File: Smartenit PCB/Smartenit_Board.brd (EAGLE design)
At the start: 55.3 x 72.5 mm, 85 parts, among them J3 2X5CONNECTOR1.27MM, Q1 QUARTZ_3.58M_2PIN, U1 ADE7953, U2 ESP-WROOM-32, U3 SN74LVC1G3157

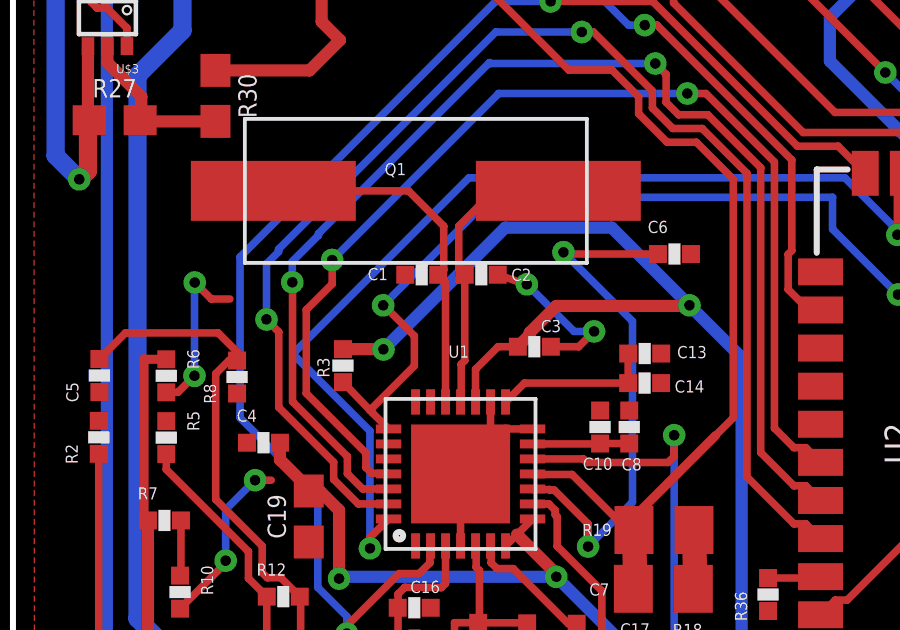
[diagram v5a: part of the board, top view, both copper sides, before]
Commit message: moved two caps
proximity issue reslved with caps by crystal.
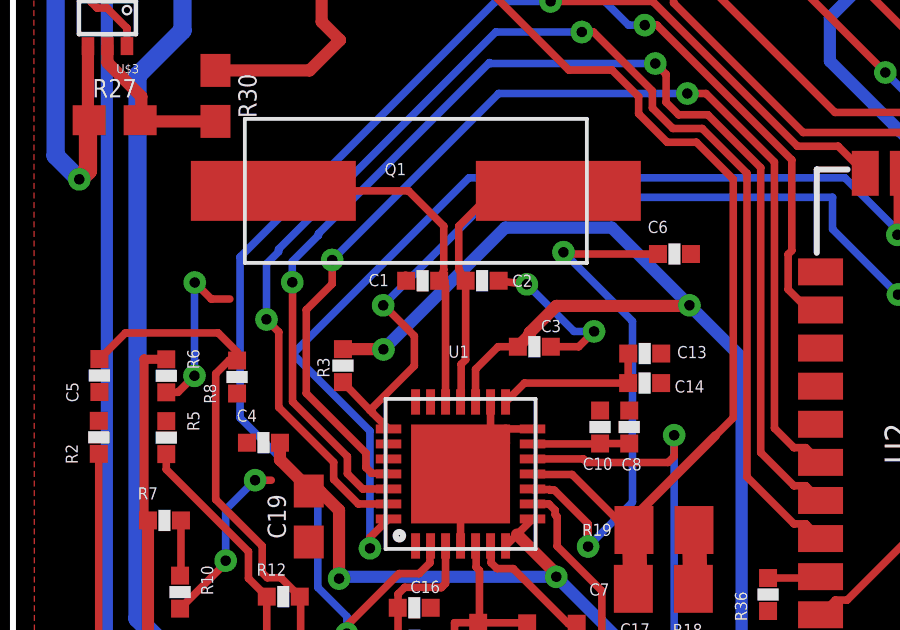
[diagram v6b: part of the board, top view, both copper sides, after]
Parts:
- moved C1 0.20 mm to (13.7, -29.2)
- moved C2 0.20 mm to (15.6, -29.2)
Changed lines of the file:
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@@
 <attribute name="NAME" x="12.39" y="-25.695" size="0.4064" layer="21"/>
 </element>
-<element name="C1" library="Nizanlib" package="0402-CAP" value="20p" x="13.626" y="-29.012" smashed="yes">
-<attribute name="NAME" x="11.827" y="-29.1935" size="0.4064" layer="25"/>
-</element>
-<element name="C2" library="Nizanlib" package="0402-CAP" value="20p" x="15.61" y="-29.01" smashed="yes" rot="R180">
-<attribute name="NAME" x="17.279" y="-28.8085" size="0.4064" layer="25" rot="R180"/>
+<element name="C1" library="Nizanlib" package="0402-CAP" value="20p" x="13.656" y="-29.212" smashed="yes">
+<attribute name="NAME" x="11.857" y="-29.3935" size="0.4064" layer="25"/>
+</element>
+<element name="C2" library="Nizanlib" package="0402-CAP" value="20p" x="15.64" y="-29.21" smashed="yes" rot="R180">
+<attribute name="NAME" x="17.309" y="-29.0085" size="0.4064" layer="25" rot="R180"/>
 </element>
 <element name="C8" library="Nizanlib" package="0402-CAP" value="475n" x="20.542" y="-34.087" smashed="yes" rot="R90">
@@
 <contactref element="Q1" pad="1"/>
 <wire x1="14.36" y1="-29.266" x2="14.196" y2="-29.102" width="0.254" layer="1"/>
-<wire x1="14.196" y1="-29.102" x2="14.176" y2="-29.012" width="0.254" layer="1"/>
+<wire x1="14.196" y1="-29.102" x2="14.206" y2="-29.212" width="0.254" layer="1"/>
 <wire x1="14.36" y1="-28.848" x2="14.36" y2="-27.39" width="0.254" layer="1"/>
-<wire x1="14.36" y1="-28.848" x2="14.176" y2="-29.012" width="0.254" layer="1"/>
+<wire x1="14.36" y1="-28.848" x2="14.206" y2="-29.212" width="0.254" layer="1"/>
 <wire x1="14.42" y1="-29.38455625" x2="14.42" y2="-33.251" width="0.254" layer="1"/>
-<wire x1="14.176" y1="-29.012" x2="14.393475" y2="-29.229475" width="0.254" layer="1"/>
+<wire x1="14.206" y1="-29.212" x2="14.393475" y2="-29.229475" width="0.254" layer="1"/>
 <wire x1="14.393475" y1="-29.229475" x2="14.393475" y2="-29.35803125" width="0.254" layer="1"/>
 <wire x1="14.393475" y1="-29.35803125" x2="14.42" y2="-29.38455625" width="0.254" layer="1"/>
@@
 <contactref element="C2" pad="2"/>
 <wire x1="14.86" y1="-28.83" x2="14.86" y2="-27.39" width="0.254" layer="1"/>
-<wire x1="14.86" y1="-28.83" x2="15.06" y2="-29.01" width="0.254" layer="1"/>
-<wire x1="14.86" y1="-29.19" x2="15.06" y2="-29.01" width="0.254" layer="1"/>
-<wire x1="15.06" y1="-29.01" x2="15.06" y2="-31.87341875" width="0.254" layer="1"/>
+<wire x1="14.86" y1="-28.83" x2="15.09" y2="-29.21" width="0.254" layer="1"/>
 <wire x1="14.9398" y1="-33.2312" x2="14.92" y2="-33.251" width="0.254" layer="1"/>
-<wire x1="15.06" y1="-31.87341875" x2="14.9398" y2="-31.99361875" width="0.254" layer="1"/>
 <wire x1="14.9398" y1="-31.99361875" x2="14.9398" y2="-33.2312" width="0.254" layer="1"/>
 <wire x1="14.86" y1="-27.39" x2="16.035" y2="-26.215" width="0.254" layer="1"/>
 <wire x1="16.035" y1="-26.215" x2="18.18" y2="-26.215" width="0.254" layer="1"/>
+<wire x1="15.09" y1="-29.21" x2="15.09" y2="-31.84341875" width="0.254" layer="1"/>
+<wire x1="15.09" y1="-31.84341875" x2="14.9398" y2="-31.99361875" width="0.254" layer="1"/>
 </signal>
 <signal name="N$7">
@@
 <contactref element="R11" pad="2"/>
 <wire x1="22.74" y1="-42.05" x2="22.62" y2="-41.93" width="0.254" layer="1"/>
-<wire x1="13.088" y1="-29.02" x2="13.076" y2="-29.012" width="0.254" layer="1"/>
+<wire x1="13.088" y1="-29.02" x2="13.106" y2="-29.212" width="0.254" layer="1"/>
 <contactref element="R1" pad="1"/>
 <contactref element="R2" pad="2"/>
@@
 <wire x1="37.74" y1="-6.53" x2="37.85" y2="-6.64" width="0.254" layer="1"/>
 <wire x1="37.85" y1="-6.64" x2="37.85" y2="-10.15" width="0.254" layer="1"/>
-<wire x1="16.16" y1="-29.01" x2="17.13" y2="-29.34" width="0.254" layer="1"/>
+<wire x1="16.19" y1="-29.21" x2="17.13" y2="-29.34" width="0.254" layer="1"/>
 <wire x1="17.13" y1="-29.34" x2="17.13" y2="-29.33" width="0.254" layer="1"/>
 <via x="17.13" y="-29.33" extent="1-16" drill="0.35"/>

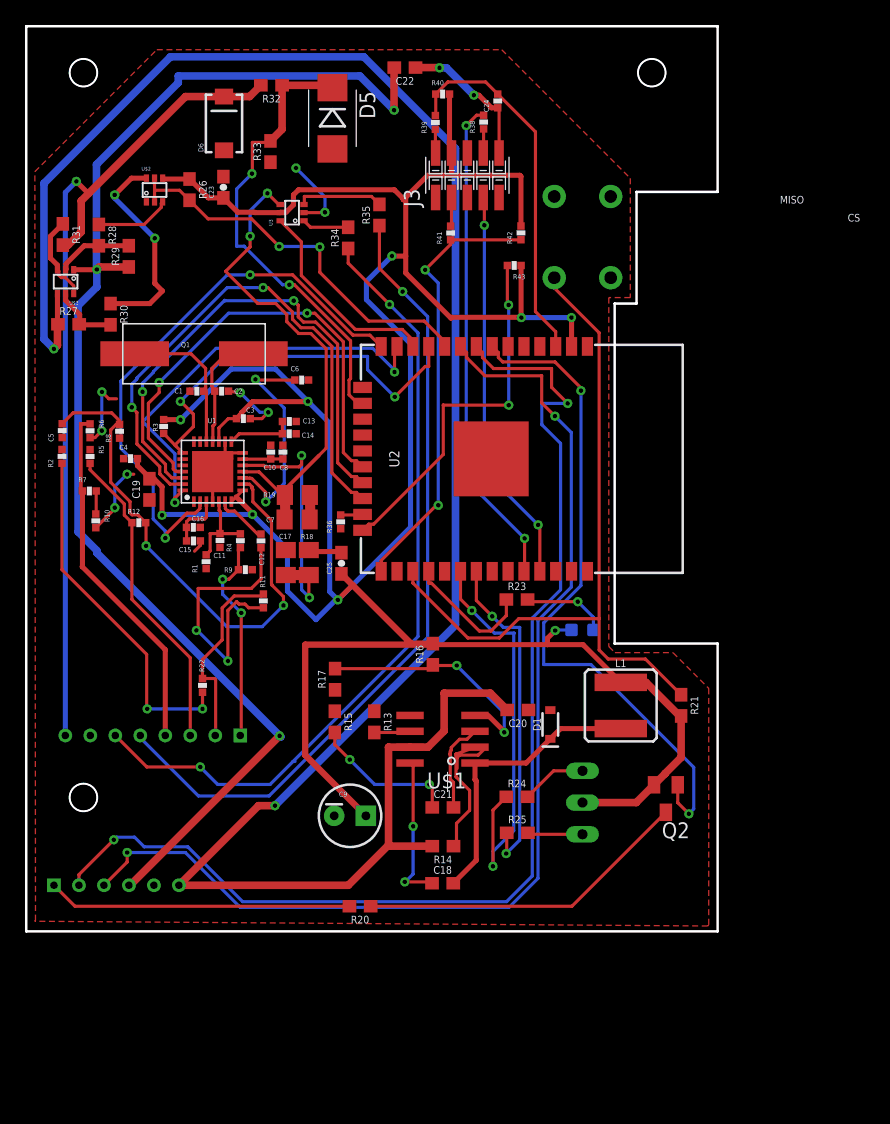
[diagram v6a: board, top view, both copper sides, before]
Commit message: changed blue LED
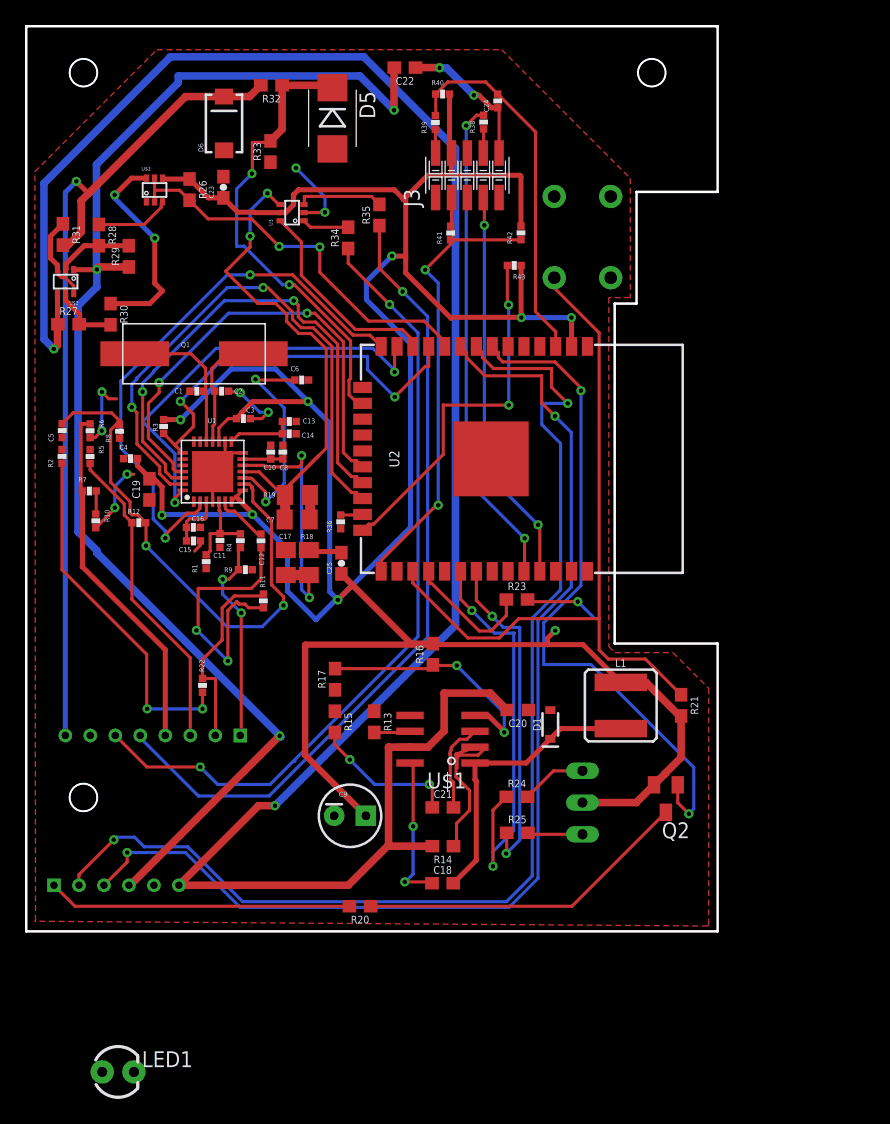
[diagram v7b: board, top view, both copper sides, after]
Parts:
- removed D2: BLUE, SparkFun-LED:LED-0603
- added LED1: (no value), SparkFun:LED3MM
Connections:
- net 3.3V: now also LED1.A; no longer D2.A
- net N$21: now also LED1.K; no longer D2.C
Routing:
- net 3.3V: track 248.6 -> 247.3 mm
- net N$21: track 6.87 -> 5.86 mm
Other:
- board text removed: "CS"
- board text removed: "MISO"
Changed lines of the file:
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@@
 <text x="17.52" y="-28.03" size="1.016" layer="26" rot="MR0">Watt Meter </text>
 <text x="17.47" y="-26.65" size="1.016" layer="26" rot="MR0">CalPlug</text>
-<text x="60.32" y="-14.19" size="0.6096" layer="25">MISO</text>
-<text x="65.75" y="-15.63" size="0.6096" layer="25">CS</text>
 <wire x1="0" y1="0" x2="0" y2="-72.45" width="0.2" layer="20"/>
 <wire x1="0" y1="-72.45" x2="55.34" y2="-72.45" width="0.2" layer="20"/>
@@
 </element>
 <element name="Q2" library="semicon-smd-ipc" library_urn="urn:adsk.eagle:library:353" package="SOT23" package3d_urn="urn:adsk.eagle:package:26310/1" value="" x="51.2" y="-61.82" rot="R180"/>
-<element name="D2" library="SparkFun-LED" package="LED-0603" value="BLUE" x="44.5236" y="-48.3232" rot="MR180">
-<attribute name="PROD_ID" value="DIO-08575" x="44.5236" y="-48.3232" size="1.778" layer="28" rot="MR180" display="off"/>
-</element>
 <element name="R21" library="SparkFun-Resistors" package="0603" value="10k" x="52.42" y="-54.36" rot="R270">
 <attribute name="PROD_ID" value="RES-00824" x="52.42" y="-54.36" size="1.778" layer="27" rot="R270" display="off"/>
@@
 <element name="U$4" library="Smart_Charger" package="CONN82MM" value="2MM_CONN8" x="3.13" y="-56.77"/>
 <element name="U$5" library="Smart_Charger" package="CONN6_2MM" value="2MM_CONN6" x="2.22" y="-68.76"/>
+<element name="LED1" library="SparkFun" package="LED3MM" value="" x="7.35" y="-83.7"/>
 </elements>
 <signals>
@@
 <wire x1="17.32" y1="-37.151" x2="17.28" y2="-37.191" width="0.254" layer="1"/>
 <wire x1="16.42" y1="-38.32" x2="16.42" y2="-38.051" width="0.254" layer="1"/>
-<contactref element="D2" pad="A"/>
 <contactref element="R21" pad="2"/>
 <contactref element="U$2" pad="4"/>
@@
 <wire x1="24.74" y1="-45.95" x2="24.97" y2="-45.95" width="0.4064" layer="16"/>
 <wire x1="20.91" y1="-41.88" x2="20.91" y2="-45.22" width="0.4064" layer="16"/>
-<wire x1="43.6466" y1="-48.3232" x2="42.3868" y2="-48.3232" width="0.254" layer="16"/>
 <wire x1="42.3868" y1="-48.3232" x2="42.34" y2="-48.37" width="0.254" layer="16"/>
 <wire x1="22.34" y1="-30.03" x2="22.55" y2="-30.03" width="0.4064" layer="1"/>
@@
 <wire x1="29.28" y1="-18.4" x2="30.375" y2="-18.4" width="0.4064" layer="1"/>
 <wire x1="30.76" y1="-40.1" x2="30.76" y2="-25.42" width="0.4064" layer="16"/>
+<contactref element="LED1" pad="A"/>
+<wire x1="27.19" y1="-63.2" x2="6.08" y2="-83.7" width="0" layer="19" extent="1-1"/>
 </signal>
 <signal name="N$22">
@@
 </signal>
 <signal name="N$21">
-<contactref element="D2" pad="C"/>
 <contactref element="R23" pad="2"/>
 <wire x1="40.13" y1="-45.89" x2="40.3" y2="-46.06" width="0.254" layer="1"/>
@@
 <via x="44.15" y="-46.06" extent="1-16" drill="0.35"/>
 <wire x1="44.15" y1="-46.06" x2="45.4006" y2="-47.3106" width="0.254" layer="16"/>
-<wire x1="45.4006" y1="-47.3106" x2="45.4006" y2="-48.3232" width="0.254" layer="16"/>
+<contactref element="LED1" pad="K"/>
+<wire x1="40.3" y1="-46.06" x2="8.62" y2="-83.7" width="0" layer="19" extent="1-1"/>
 </signal>
 <signal name="N$25">

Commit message: Finished Routing
Finished aligning dimensions, routing, fixing trace sizes and fixed cap on 12V line.
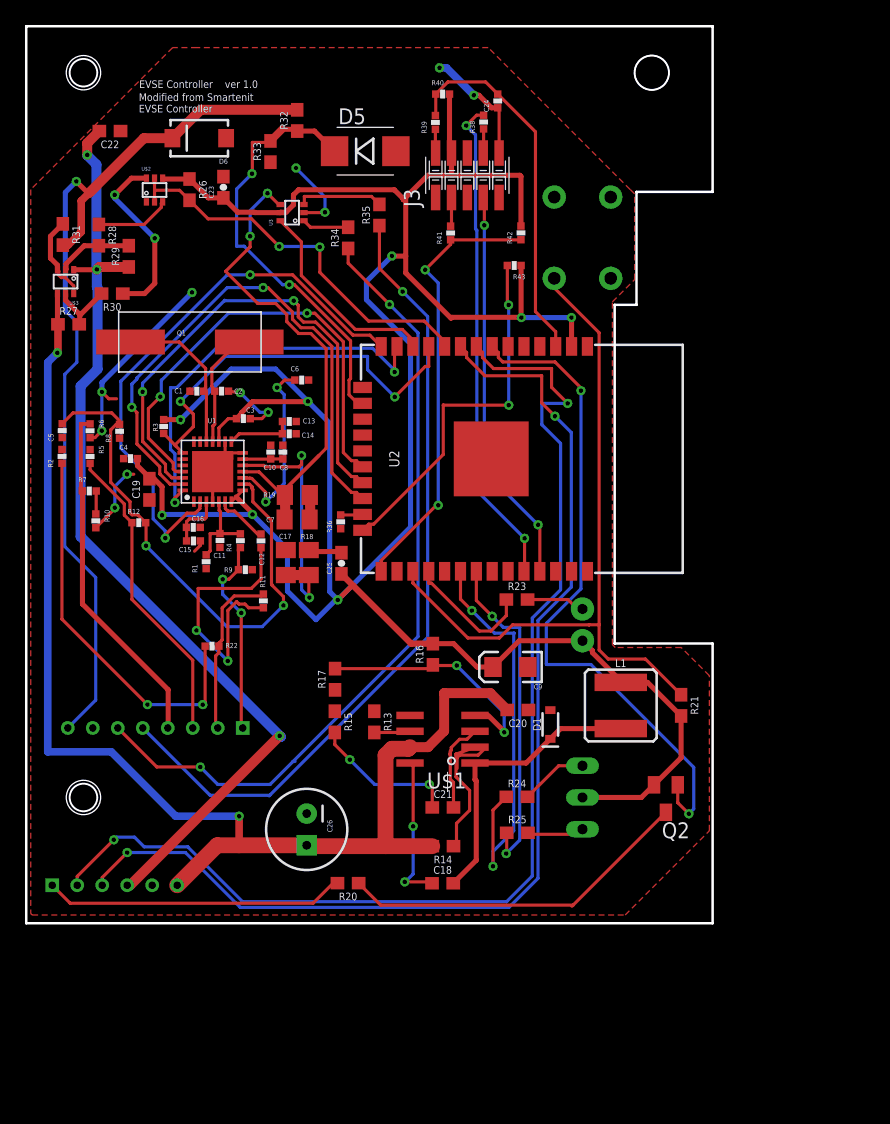
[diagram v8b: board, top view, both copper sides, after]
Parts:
- added C26: (no value), SparkFun:CPOL-RADIAL-100UF-25V
- C9: device SparkFun:CPOL-RADIAL-10UF-25V -> SparkFun:EIA3216
- moved LED1 51.6 mm to (44.5, -47.9), flipped to the bottom, turned to 90 degrees
- moved C22 24.2 mm to (6.70, -8.39)
- moved C9 17.5 mm to (38.8, -51.3), turned to 180 degrees
- moved D5 3.72 mm to (27.1, -10.0), turned to 0 degrees
- moved R32 3.48 mm to (21.7, -7.54), turned to 90 degrees
- moved R22 3.23 mm to (14.9, -49.6), turned to 180 degrees
- moved D6 2.30 mm to (13.8, -8.96), turned to 180 degrees
- moved R20 2.08 mm to (25.8, -68.6)
- moved R30 1.66 mm to (6.88, -21.4), turned to 180 degrees
- moved Q1 1.00 mm to (13.1, -25.3)
- moved U$4 0.63 mm to (3.33, -56.2)
- moved LD1 0.41 mm to (44.5, -61.7)
- moved U$5 0.14 mm to (2.08, -68.8)
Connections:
- net 12V: now also C26.1
- net 3.3V: now also C9.A; no longer C9.1
- net GND: now also C26.2, C9.C; no longer C9.2
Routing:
- net 12V: track 170.4 -> 100.2 mm
- net -12V: track 106.8 -> 78.5 mm
- net 3.3V: track 247.3 -> 221.8 mm, vias 9 -> 8
- net GND: track 72.8 -> 81.8 mm, vias 12 -> 13
- net PILOT: track 68.7 -> 73.3 mm
- net N$27: track 28.2 -> 31.3 mm
- net N$13: track 17.8 -> 15.1 mm
- net ADC1: track 37.3 -> 34.6 mm
- net N$32: track 16.9 -> 14.4 mm
- net IAN: track 15.6 -> 13.6 mm
- net N$20: track 26.7 -> 28.5 mm
- net DIO0: track 34.4 -> 32.8 mm
- net N$2: track 9.80 -> 11.1 mm
- net N$21: track 5.86 -> 4.71 mm, vias 1 -> 0
- net N$1: track 12.6 -> 13.3 mm
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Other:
- board size 55.3 x 72.5 mm -> 54.9 x 71.8 mm
- board text added: "EVSE Controller ver 1.0"
- board text added: "Modified from Smartenit EVSE Controller"
- board text removed: "CalPlug"
- board text removed: "Watt Meter"
